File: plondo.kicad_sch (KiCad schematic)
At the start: 31 parts, among them J1 AVR_TC2030, J2 USB4085, U1 ATmega32A-P, Y1 Crystal

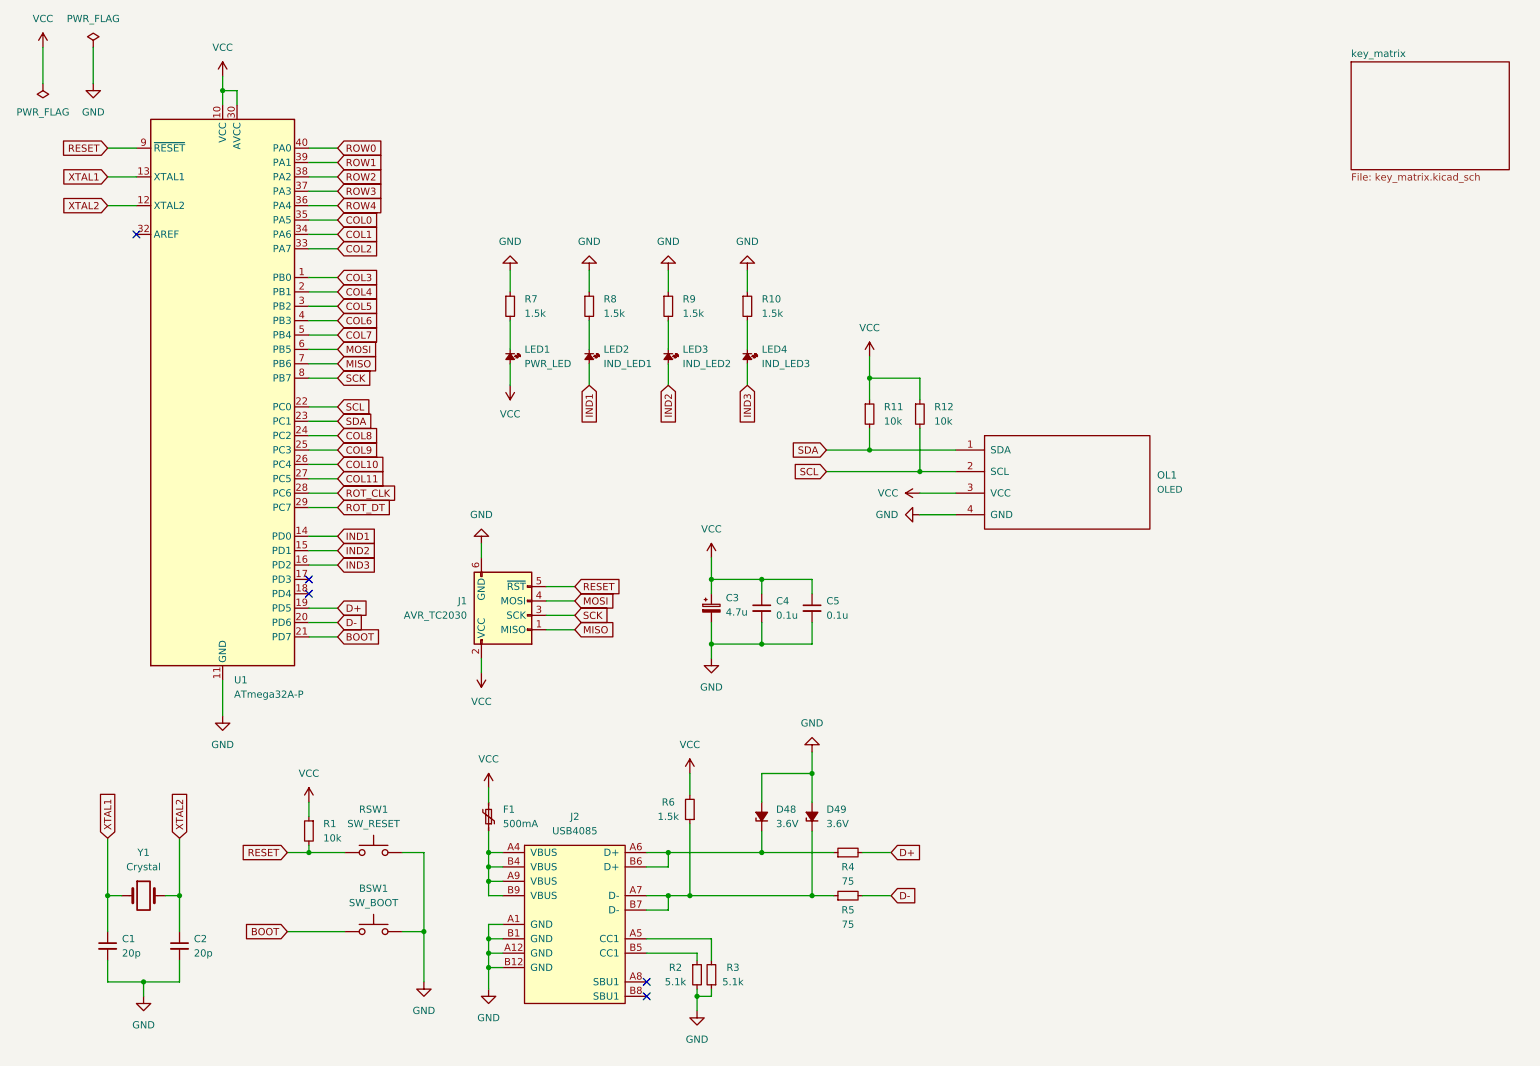
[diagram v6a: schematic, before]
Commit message: edited schematics for clarity, position more of pcb
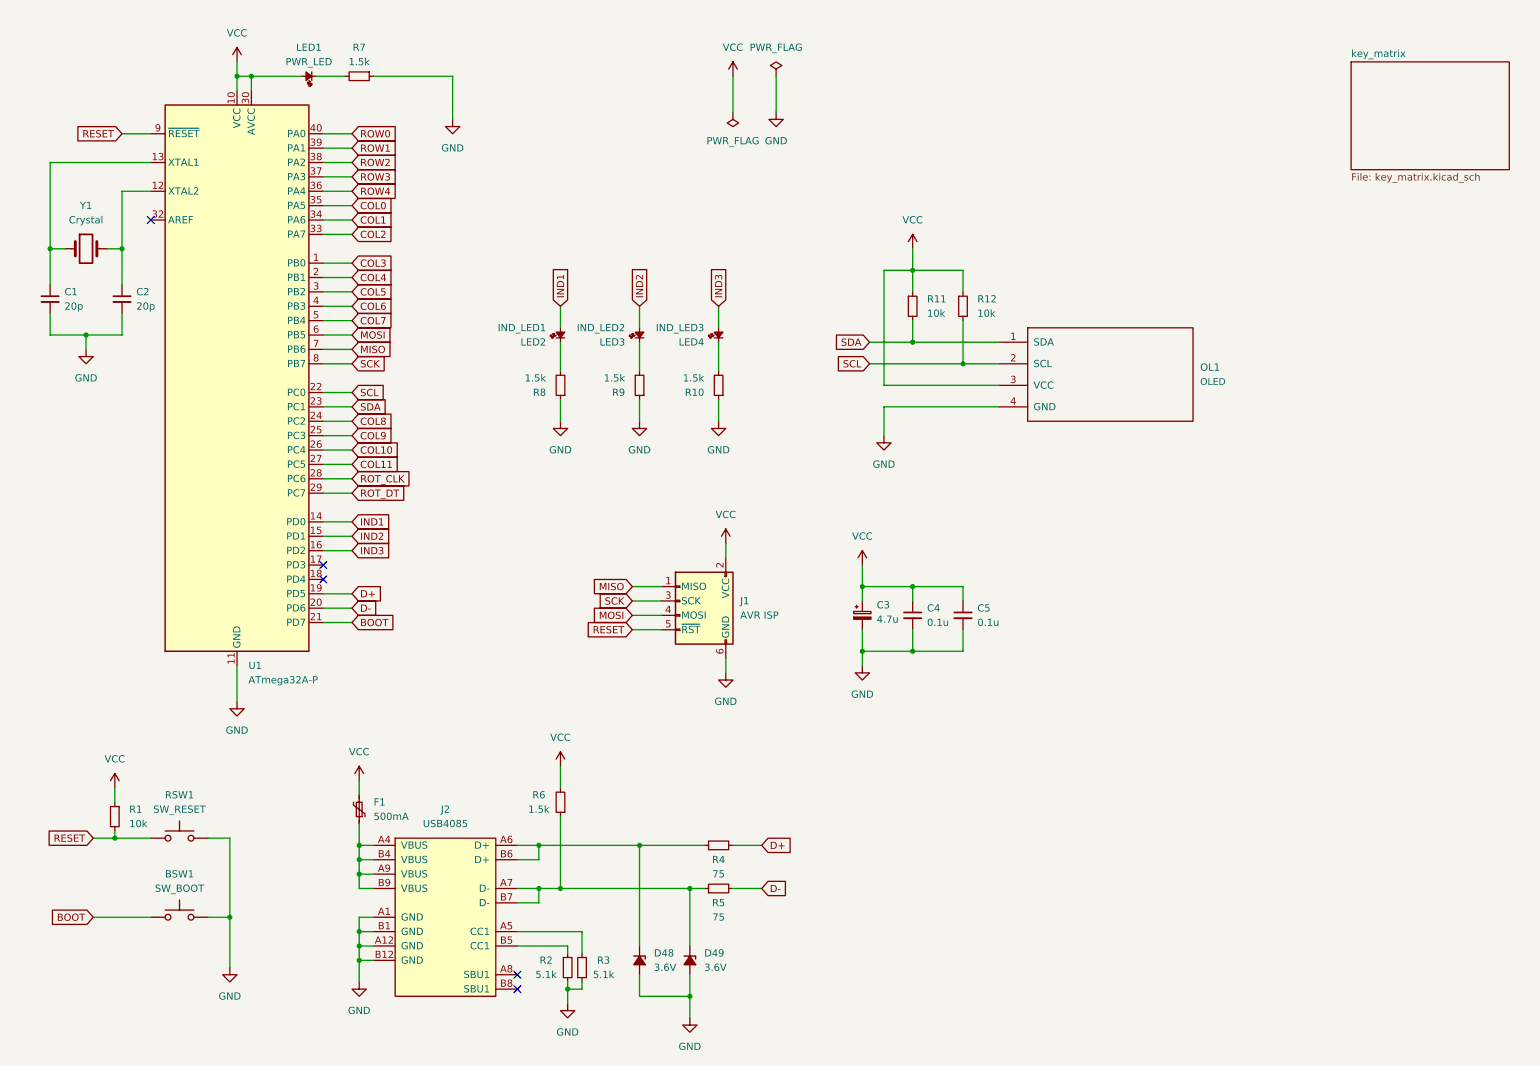
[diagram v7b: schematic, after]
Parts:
- J1: value AVR_TC2030 -> AVR ISP
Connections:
- net XTAL1: no longer names the net of C1.1, U1.13 (XTAL1), Y1.1
- net XTAL2: no longer names the net of C2.1, U1.12 (XTAL2), Y1.2
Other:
- moved on the sheet: BSW1, C1, C2, C3, C4, C5, D48, D49, F1, J1, J2, LED1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

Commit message: rearrange pins + misc pcb arrangement fixes
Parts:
- J1: footprint Connector_PinHeader_1.27mm:PinHeader_2x03_P1.27mm_Vertical -> Connector_PinHeader_2.54mm:PinHeader_2x03_P2.54mm_Vertical
- OL1: footprint kbd:OLED_1side -> kbd:OLED_v2
- Y1: value Crystal -> 16MHz
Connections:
- net ROT_CLK is gone; now on net COL1: U1.28 (PC6)
- net ROT_DT is gone; now on net COL2: U1.29 (PC7)
- net BOOT: now also U1.17 (PD3); no longer U1.21 (PD7)
- net COL0: now also U1.27 (PC5); no longer U1.35 (PA5)
- net COL1: no longer U1.34 (PA6)
- net COL10: now also U1.40 (PA0); no longer U1.26 (PC4)
- net COL11: now also U1.14 (PD0); no longer U1.27 (PC5)
- net COL2: no longer U1.33 (PA7)
- net COL3: now also U1.33 (PA7); no longer U1.1 (PB0)
- net COL4: now also U1.34 (PA6); no longer U1.2 (PB1)
- net COL5: now also U1.35 (PA5); no longer U1.3 (PB2)
- net COL6: now also U1.36 (PA4); no longer U1.4 (PB3)
- net COL7: now also U1.37 (PA3); no longer U1.5 (PB4)
- net COL8: now also U1.38 (PA2); no longer U1.24 (PC2)
- net COL9: now also U1.39 (PA1); no longer U1.25 (PC3)
- net D+: now also U1.1 (PB0); no longer U1.19 (PD5)
- net D-: now also U1.2 (PB1); no longer U1.20 (PD6)
- net IND1: now also U1.18 (PD4); no longer U1.14 (PD0)
- net IND2: now also U1.19 (PD5); no longer U1.15 (PD1)
- net IND3: now also U1.20 (PD6); no longer U1.16 (PD2)
- net ROW0: now also U1.5 (PB4); no longer U1.40 (PA0)
- net ROW1: now also U1.21 (PD7); no longer U1.39 (PA1)
- net ROW2: now also U1.24 (PC2); no longer U1.38 (PA2)
- net ROW3: now also U1.25 (PC3); no longer U1.37 (PA3)
- net ROW4: now also U1.26 (PC4); no longer U1.36 (PA4)
- new net ROT_A: U1.3 (PB2)
- new net ROT_B: U1.4 (PB3)
